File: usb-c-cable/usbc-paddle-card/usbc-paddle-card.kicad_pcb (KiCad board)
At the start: 2 copper layers, 7 x 9 mm, 7 parts, among them J1 USB_C_Receptacle, P1 PAD_SMD, P2 PAD_SMD, P3 PAD_SMD, P4 PAD_SMD, P5 PAD_SMD

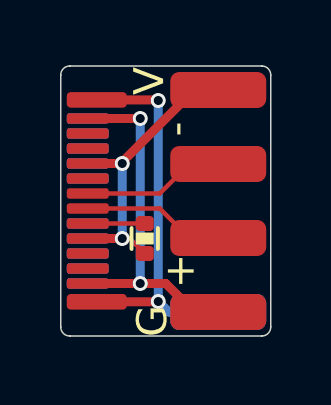
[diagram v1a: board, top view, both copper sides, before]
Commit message: Added resistor for Up-Stream use.
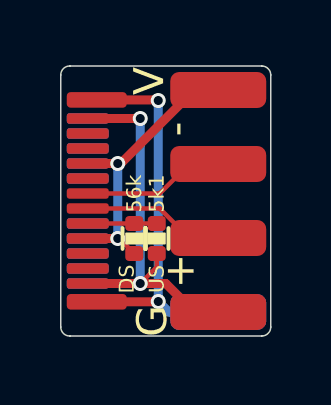
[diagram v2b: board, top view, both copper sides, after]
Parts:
- added R2: 5k1, pkl_dipol:R_0402, F.Cu at (32.2, 31.2)
- moved R1 0.35 mm to (31.4, 31.2)
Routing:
- net GND: track 15.8 -> 17.1 mm
- net VBUS: track 12.7 -> 12.0 mm
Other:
- board text added: "56k"
- board text added: "5k1"
- board text added: "DS"
- board text added: "US"
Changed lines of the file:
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@@
-(kicad_pcb (version 20201115) (generator pcbnew)
+(kicad_pcb (version 20201116) (generator pcbnew)
   (general
     (thickness 1)
@@
   (footprint "pkl_pads:PAD_SMD_1.2x2.5" (layer "F.Cu")
     (at 34.6 33.7)
-    (property "Sheet file" "usbc-breakout.kicad_sch")
+    (property "Sheet file" "usbc-paddle-card.kicad_sch")
     (property "Sheet name" "")
     (attr exclude_from_pos_files)
@@
   (footprint "pkl_pads:PAD_SMD_1.2x2.5" (layer "F.Cu")
     (at 34.6 31.233332)
-    (property "Sheet file" "usbc-breakout.kicad_sch")
+    (property "Sheet file" "usbc-paddle-card.kicad_sch")
     (property "Sheet name" "")
     (attr exclude_from_pos_files)
@@
   (footprint "pkl_pads:PAD_SMD_1.2x2.5" (layer "F.Cu")
     (at 34.6 26.3)
-    (property "Sheet file" "usbc-breakout.kicad_sch")
+    (property "Sheet file" "usbc-paddle-card.kicad_sch")
     (property "Sheet name" "")
     (attr exclude_from_pos_files)
@@
     (pad "1" smd roundrect (at -0.35 0) (size 3.2 1.2) (layers "F.Cu" "F.Mask") (roundrect_rratio 0.25)
       (net 5 "VBUS") (pinfunction "PAD"))
+  )
+  (footprint "pkl_dipol:R_0402" (layer "F.Cu")
+    (at 32.2 31.25 -90)
+    (descr "Resistor SMD 0402, reflow soldering")
+    (tags "resistor 0402")
+    (property "Sheet file" "usbc-paddle-card.kicad_sch")
+    (property "Sheet name" "")
+    (attr smd)
+    (fp_text reference "R2" (at 0 -1.1 90) (layer "F.Fab")
+      (effects (font (size 0.635 0.635) (thickness 0.1)))
+    )
+    (fp_text value "5k1" (at 0 1.2 90) (layer "F.Fab")
+      (effects (font (size 0.635 0.635) (thickness 0.1)))
+    )
+    (fp_line (start 0.35 0.39) (end -0.35 0.39) (layer "F.SilkS") (width 0.13))
+    (fp_line (start -0.35 -0.39) (end 0.35 -0.39) (layer "F.SilkS") (width 0.13))
+    (fp_poly (pts (xy -0.175 0.275)
+      (xy -0.175 -0.275)
+      (xy 0.175 -0.275)
+      (xy 0.175 0.275)
+      (xy -0.1 0.275)) (layer "F.SilkS") (width 0.05) (fill solid))
+    (fp_line (start -0.95 -0.5) (end -0.95 0.5) (layer "F.CrtYd") (width 0.05))
+    (fp_line (start -0.95 0.5) (end 0.95 0.5) (layer "F.CrtYd") (width 0.05))
+    (fp_line (start 0.95 -0.5) (end 0.95 0.5) (layer "F.CrtYd") (width 0.05))
+    (fp_line (start -0.95 -0.5) (end 0.95 -0.5) (layer "F.CrtYd") (width 0.05))
+    (pad "1" smd roundrect (at -0.5 0 270) (size 0.5 0.6) (layers "F.Cu" "F.Paste" "F.Mask") (roundrect_rratio 0.25)
+      (net 13 "Net-(J1-PadA5)"))
+    (pad "2" smd roundrect (at 0.5 0 270) (size 0.5 0.6) (layers "F.Cu" "F.Paste" "F.Mask") (roundrect_rratio 0.25)
+      (net 2 "GND"))
+    (model "${KISYS3DMOD}/Resistor_SMD.3dshapes/R_0402_1005Metric.step"
+      (offset (xyz 0 0 0))
+      (scale (xyz 1 1 1))
+      (rotate (xyz 0 0 0))
+    )
   )
   (footprint "pkl_connectors:USB_C_Plug_CNC_C-AW10-AK5V50" (layer "F.Cu")
@@
     (descr "Universal Serial Bus (USB) Shielded I/O Plug, Type C, Right Angle, Surface Mount, http://www.molex.com/pdm_docs/sd/1054440001_sd.pdf")
     (tags "USB Type-C Plug Edge Mount")
-    (property "Sheet file" "usbc-breakout.kicad_sch")
+    (property "Sheet file" "usbc-paddle-card.kicad_sch")
     (property "Sheet name" "")
     (attr smd)
@@
   )
   (footprint "pkl_dipol:R_0402" (layer "F.Cu")
-    (at 31.8 31.25 -90)
+    (at 31.45 31.25 -90)
     (descr "Resistor SMD 0402, reflow soldering")
     (tags "resistor 0402")
-    (property "Sheet file" "usbc-breakout.kicad_sch")
+    (property "Sheet file" "usbc-paddle-card.kicad_sch")
     (property "Sheet name" "")
     (attr smd)
@@
       (effects (font (size 0.635 0.635) (thickness 0.1)))
     )
-    (fp_line (start -0.35 -0.44) (end 0.35 -0.44) (layer "F.SilkS") (width 0.13))
-    (fp_line (start 0.35 0.44) (end -0.35 0.44) (layer "F.SilkS") (width 0.13))
+    (fp_line (start 0.35 0.39) (end -0.35 0.39) (layer "F.SilkS") (width 0.13))
+    (fp_line (start -0.35 -0.39) (end 0.35 -0.39) (layer "F.SilkS") (width 0.13))
     (fp_poly (pts (xy -0.175 0.275)
       (xy -0.175 -0.275)
@@
   (footprint "pkl_pads:PAD_SMD_1.2x2.5" (layer "F.Cu")
     (at 34.6 28.766666)
-    (property "Sheet file" "usbc-breakout.kicad_sch")
+    (property "Sheet file" "usbc-paddle-card.kicad_sch")
     (property "Sheet name" "")
     (attr exclude_from_pos_files)
@@
   (footprint "pkl_pads:PAD_SMD_1.2x2.5" (layer "B.Cu")
     (at 34.6 33.7 180)
-    (property "Sheet file" "usbc-breakout.kicad_sch")
+    (property "Sheet file" "usbc-paddle-card.kicad_sch")
     (property "Sheet name" "")
     (attr exclude_from_pos_files)
@@
     (effects (font (size 1 1) (thickness 0.15)))
   )
+  (gr_text "5k1" (at 32.2 29.75 90) (layer "F.SilkS")
+    (effects (font (size 0.5 0.5) (thickness 0.1)))
+  )
+  (gr_text "DS" (at 31.2 32.6 90) (layer "F.SilkS")
+    (effects (font (size 0.5 0.5) (thickness 0.1)))
+  )
   (gr_text "G" (at 32.05 34 90) (layer "F.SilkS")
     (effects (font (size 1 1) (thickness 0.15)))
   )
+  (gr_text "US" (at 32.2 32.6 90) (layer "F.SilkS")
+    (effects (font (size 0.5 0.5) (thickness 0.1)))
+  )
   (gr_text "+\n" (at 33 32.3) (layer "F.SilkS")
     (effects (font (size 1 1) (thickness 0.15)))
+  )
+  (gr_text "56k" (at 31.45 29.75 90) (layer "F.SilkS")
+    (effects (font (size 0.5 0.5) (thickness 0.1)))
   )
   (gr_text "-" (at 32.85 27.6 90) (layer "F.SilkS")
@@
   (segment (start 33.45 33.7) (end 34.6 33.7) (width 0.3) (layer "F.Cu") (net 2))
   (segment (start 29.9 27.25) (end 31.65 27.25) (width 0.3) (layer "F.Cu") (net 2))
+  (segment (start 32.2 31.75) (end 32.2 32.2) (width 0.15) (layer "F.Cu") (net 2))
   (segment (start 29.9 32.75) (end 31.65 32.75) (width 0.3) (layer "F.Cu") (net 2))
   (segment (start 31.65 32.75) (end 32.5 32.75) (width 0.3) (layer "F.Cu") (net 2))
+  (segment (start 32.2 32.2) (end 31.65 32.75) (width 0.15) (layer "F.Cu") (net 2))
   (segment (start 32.5 32.75) (end 33.45 33.7) (width 0.3) (layer "F.Cu") (net 2))
   (via (at 31.65 27.25) (size 0.5) (drill 0.3) (layers "F.Cu" "B.Cu") (net 2))
@@
   (segment (start 29.9 27.25) (end 31.65 27.25) (width 0.3) (layer "B.Cu") (net 2))
   (segment (start 29.9 32.75) (end 31.65 32.75) (width 0.3) (layer "B.Cu") (net 2))
-  (segment (start 31.05 28.75) (end 31.05 28.7) (width 0.3) (layer "F.Cu") (net 5))
-  (segment (start 29.9 28.75) (end 31.05 28.75) (width 0.3) (layer "F.Cu") (net 5))
-  (segment (start 29.9 31.25) (end 31.05 31.25) (width 0.3) (layer "F.Cu") (net 5))
+  (segment (start 30.9 31.25) (end 30.95 31.25) (width 0.15) (layer "F.Cu") (net 5))
+  (segment (start 30.9 28.75) (end 31 28.75) (width 0.3) (layer "F.Cu") (net 5))
   (segment (start 33.45 26.3) (end 34.6 26.3) (width 0.3) (layer "F.Cu") (net 5))
-  (segment (start 31.3 31.25) (end 31.05 31.25) (width 0.15) (layer "F.Cu") (net 5))
-  (segment (start 31.05 28.7) (end 33.45 26.3) (width 0.3) (layer "F.Cu") (net 5))
-  (segment (start 31.8 31.75) (end 31.3 31.25) (width 0.15) (layer "F.Cu") (net 5))
-  (via (at 31.05 28.75) (size 0.5) (drill 0.3) (layers "F.Cu" "B.Cu") (net 5))
-  (via (at 31.05 31.25) (size 0.5) (drill 0.3) (layers "F.Cu" "B.Cu") (net 5))
-  (segment (start 29.9 31.25) (end 31.05 31.25) (width 0.3) (layer "B.Cu") (net 5))
-  (segment (start 31.05 31.25) (end 31.05 28.75) (width 0.3) (layer "B.Cu") (net 5))
-  (segment (start 29.9 28.75) (end 31.05 28.75) (width 0.3) (layer "B.Cu") (net 5))
+  (segment (start 29.9 28.75) (end 30.9 28.75) (width 0.3) (layer "F.Cu") (net 5))
+  (segment (start 30.95 31.25) (end 31.45 31.75) (width 0.15) (layer "F.Cu") (net 5))
+  (segment (start 31 28.75) (end 33.45 26.3) (width 0.3) (layer "F.Cu") (net 5))
+  (segment (start 29.9 31.25) (end 30.9 31.25) (width 0.3) (layer "F.Cu") (net 5))
+  (via (at 30.9 31.25) (size 0.5) (drill 0.3) (layers "F.Cu" "B.Cu") (net 5))
+  (via (at 30.9 28.75) (size 0.5) (drill 0.3) (layers "F.Cu" "B.Cu") (net 5))
+  (segment (start 29.9 28.75) (end 30.9 28.75) (width 0.3) (layer "B.Cu") (net 5))
+  (segment (start 29.9 31.25) (end 30.9 31.25) (width 0.3) (layer "B.Cu") (net 5))
   (segment (start 29.9 31.25) (end 29.82499 31.25) (width 0.3) (layer "B.Cu") (net 5))
-  (segment (start 31.75 30.75) (end 31.8 30.7) (width 0.15) (layer "F.Cu") (net 13))
-  (segment (start 29.9 30.75) (end 31.8 30.75) (width 0.15) (layer "F.Cu") (net 13))
+  (segment (start 30.9 28.75) (end 30.9 31.25) (width 0.3) (layer "B.Cu") (net 5))
+  (segment (start 31.45 30.75) (end 32.2 30.75) (width 0.15) (layer "F.Cu") (net 13))
+  (segment (start 29.9 30.75) (end 31.45 30.75) (width 0.15) (layer "F.Cu") (net 13))
   (segment (start 29.9 29.75) (end 32.3 29.75) (width 0.15) (layer "F.Cu") (net 16))
   (segment (start 32.3 29.75) (end 33.283334 28.766666) (width 0.15) (layer "F.Cu") (net 16))

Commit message: Added revision, copyright and license notes.
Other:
- board text added: "USB-C 2.0 Paddle Card 1BitSquared CC-BY-SA"
- board text removed: "USB-C 2.0 Paddle Card 1BitSquared"
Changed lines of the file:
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@@
   )
   (paper "A4")
+  (title_block
+    (title "USB-C Paddle Card")
+    (rev "R1")
+    (company "1BitSquared")
+    (comment 1 "(C) 2020 1BitSquared <info@1bitsquared.com>")
+    (comment 2 "(C) 2020 Piotr Esden-Tempski <piotr@esden.net>")
+  )
   (layers
     (0 "F.Cu" signal)
@@
   (gr_line (start 29.3 25.5) (end 35.7 25.5) (layer "Edge.Cuts") (width 0.05))
   (gr_arc (start 35.7 25.8) (end 36 25.8) (angle -90) (layer "Edge.Cuts") (width 0.05))
-  (gr_text "USB-C  2.0\nPaddle Card\n1BitSquared" (at 34.3 30 90) (layer "B.SilkS")
+  (gr_text "USB-C  2.0\nPaddle Card\n1BitSquared\nCC-BY-SA" (at 34.25 30 90) (layer "B.SilkS")
     (effects (font (size 0.5 0.5) (thickness 0.1)) (justify mirror))
   )
